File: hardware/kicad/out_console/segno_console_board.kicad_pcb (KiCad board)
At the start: 2 copper layers, 115 x 96 mm, 53 parts, among them J1 RaspberryPi_Pico_SMD_HandSold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, J10 JST_XH_B2B-XH-A_1x02_P2.50mm_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, J11 JST_XH_B2B-XH-A_1x02_P2.50mm_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, J12 JST_XH_B2B-XH-A_1x02_P2.50mm_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, J13 JST_XH_B2B-XH-A_1x02_P2.50mm_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, J14 JST_XH_B2B-XH-A_1x02_P2.50mm_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, J15 JST_XH_B2B-XH-A_1x02_P2.50mm_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, J16 JST_XH_B2B-XH-A_1x02_P2.50mm_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, J17 JST_XH_B2B-XH-A_1x02_P2.50mm_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, J18 JST_XH_B2B-XH-A_1x02_P2.50mm_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, J19 JST_XH_B2B-XH-A_1x02_P2.50mm_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, J2 IDC-Header_2x20_P2.54mm_Verti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, J20 JST_XH_B3B-XH-A_1x03_P2.50mm_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, J21 JST_XH_B3B-XH-A_1x03_P2.50mm_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, J22 PinHeader_2x04_P2.54mm_Vertic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, J3 JST_XH_B4B-XH-A_1x04_P2.50mm_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, J4 JST_XH_B3B-XH-A_1x03_P2.50mm_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, J5 JST_XH_B2B-XH-A_1x02_P2.50mm_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, J6 JST_XH_B8B-XH-A_1x08_P2.50mm_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, J7 JST_XH_B3B-XH-A_1x03_P2.50mm_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, J8 JST_XH_B2B-XH-A_1x02_P2.50mm_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, U1 DIP-14_W7.62mm, U2 DIP-6_W7.62mm

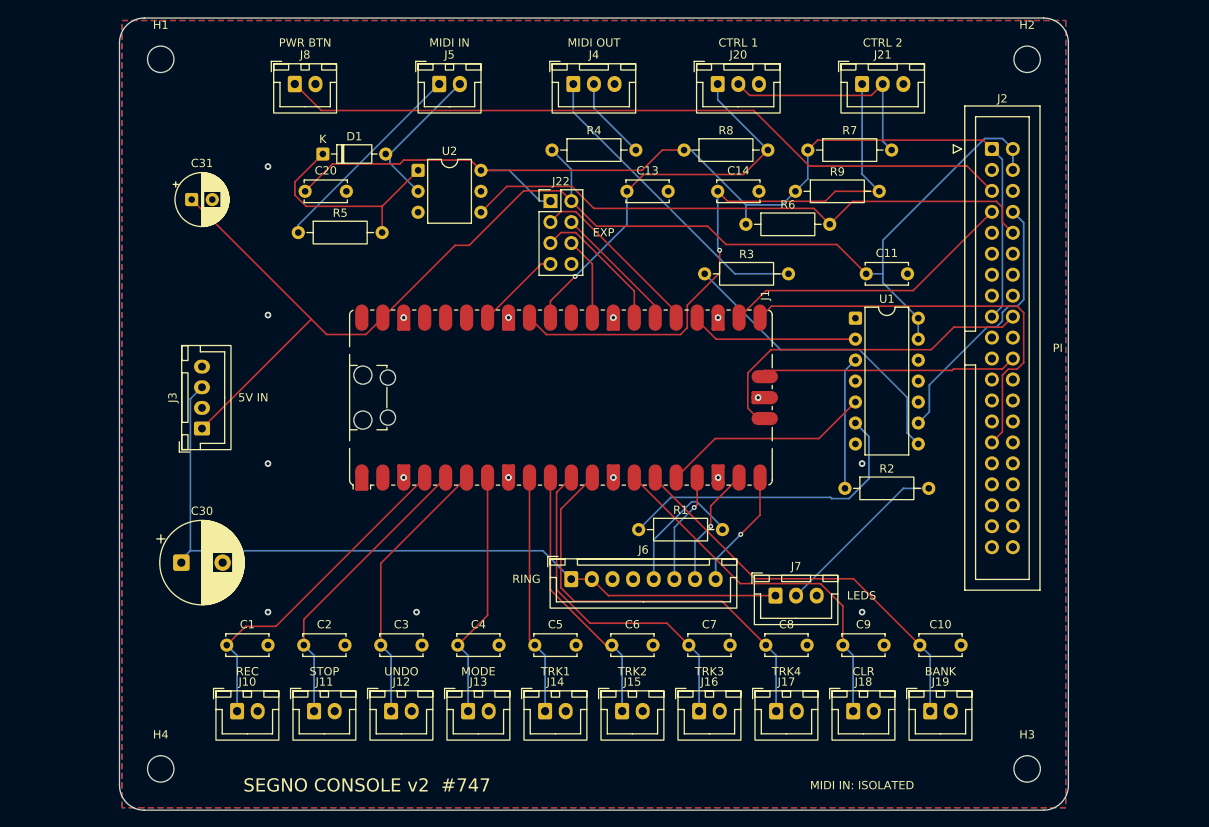
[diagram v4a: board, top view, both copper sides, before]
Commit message: fix(hardware): give the ground pours thermal relief now the Pico is SMD
The pours tied pads with solid copper. That was justified in a comment reading
"THT parts here are hand-soldered, so the usual thermal-relief argument
(wave/reflow) is moot" -- true when written, and false from the commit that made
the Pico a surface-mount module. Its nine GND pads sat in a plane on their own
layer with solid ties, which wicks the iron's heat into the plane and cold-joints
the one part that is painful to rework.

Solid was originally chosen to escape five "starved_thermal" errors from spokes
too narrow to form. That was a symptom of leaving the widths at their defaults,
not a reason to abandon relief: set explicitly (0.3 mm gap, 0.4 mm spokes) there
are none.

Two consequences, both real rather than cosmetic:
- Relief stops pads bridging the pour, which orphaned an F.Cu region. Stitch
  pitch drops 18 -> 12 mm (66 -> 83 vias). Relief and stitch pitch are one
  decision, not two.
- A 3 mm2 minimum island area drops slivers that reach a single pad and go
  nowhere; they cannot carry a return and they fail DRC as starved thermals.

Gated: any pour that ties pads solid while the board carries SMD pads now fails.
Nothing caught this transition, which is why it survived a footprint change.

0 DRC violations, 0 unconnected.

Refs #747
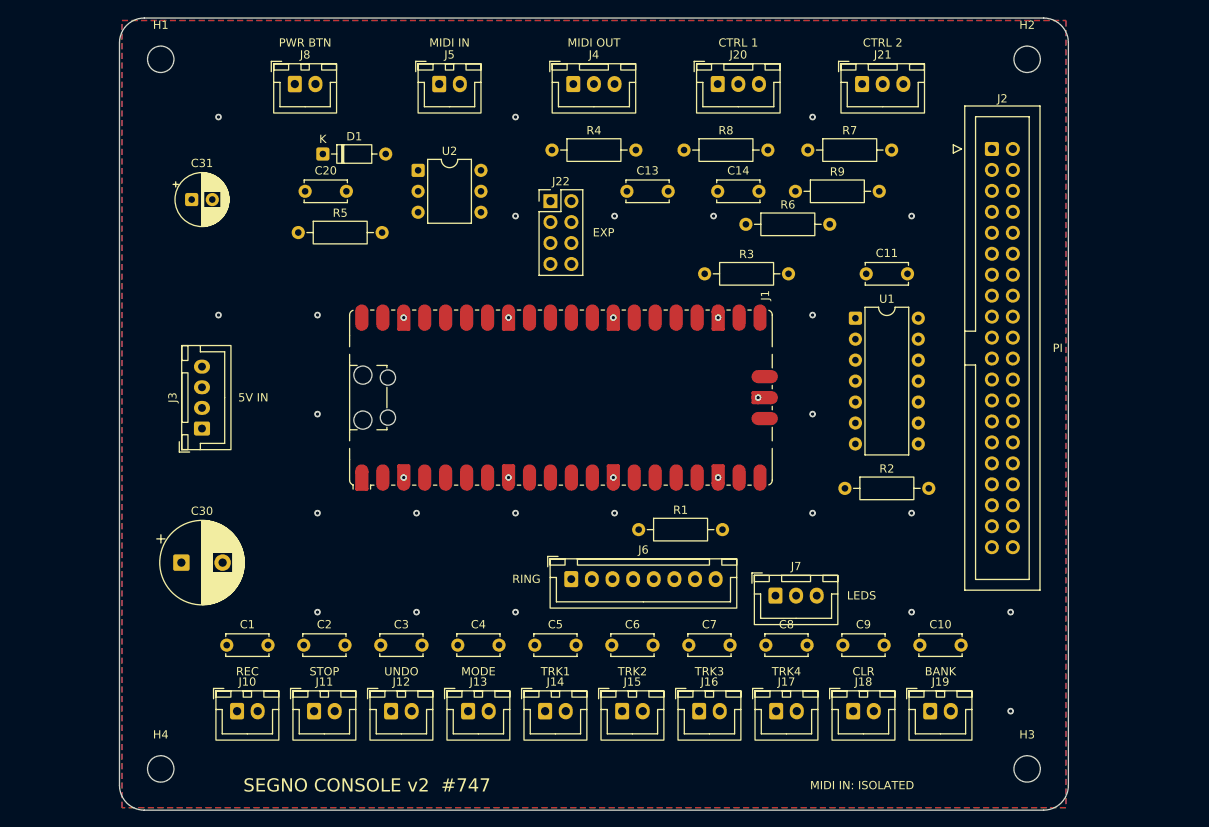
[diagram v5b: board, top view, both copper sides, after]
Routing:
- net +5V: track 165.5 -> 0.00 mm
- net +3V3: track 128.5 -> 0.00 mm
- net +5V_LED: track 95.4 -> 0.00 mm
- net PWR_BTN: track 89.8 -> 0.00 mm
- net CTRL2_TIP: track 73.0 -> 0.00 mm, vias 1 -> 0
- net MIDI_RX: track 71.5 -> 0.00 mm
- net SW_TRACK4: track 51.2 -> 0.00 mm
- net LINK_TX: track 50.8 -> 0.00 mm
- net SW_BANK: track 49.1 -> 0.00 mm
- net CTRL1_TIP: track 48.8 -> 0.00 mm, vias 1 -> 0
- net SW_CLEAR: track 45.0 -> 0.00 mm
- net SW_TRACK3: track 41.7 -> 0.00 mm
- net SWCLK: track 41.0 -> 0.00 mm
- net SW_RECPLAY: track 40.9 -> 0.00 mm
- net RING_DATA_BUF: track 38.0 -> 0.00 mm
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
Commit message: fix(hardware): keep the module's USB corridor clear, and align J6 with J7
The 5 V inlet sat directly in front of the Pico's USB socket. The argument for
pointing that end into the bulk caps was that USB is not NEEDED -- VSYS is fed
from J3 and the Pi flashes over SWD -- but "not needed" quietly became "made
impossible", which is a different claim and not one anyone agreed to. J3 moves
down the left edge and C30 moves up, leaving y 40..52 clear from the socket to
the board edge.

Gated, with a negative control that reproduces exactly the shipped mistake:
anything intruding on the corridor off the module's USB end now fails.

Also J6 (RING) and J7 (LEDS) sat at y 68 and 70 -- same footprint family, side by
side, two millimetres apart for no reason. Both on 69.

0 DRC violations, 0 unconnected.

Refs #747
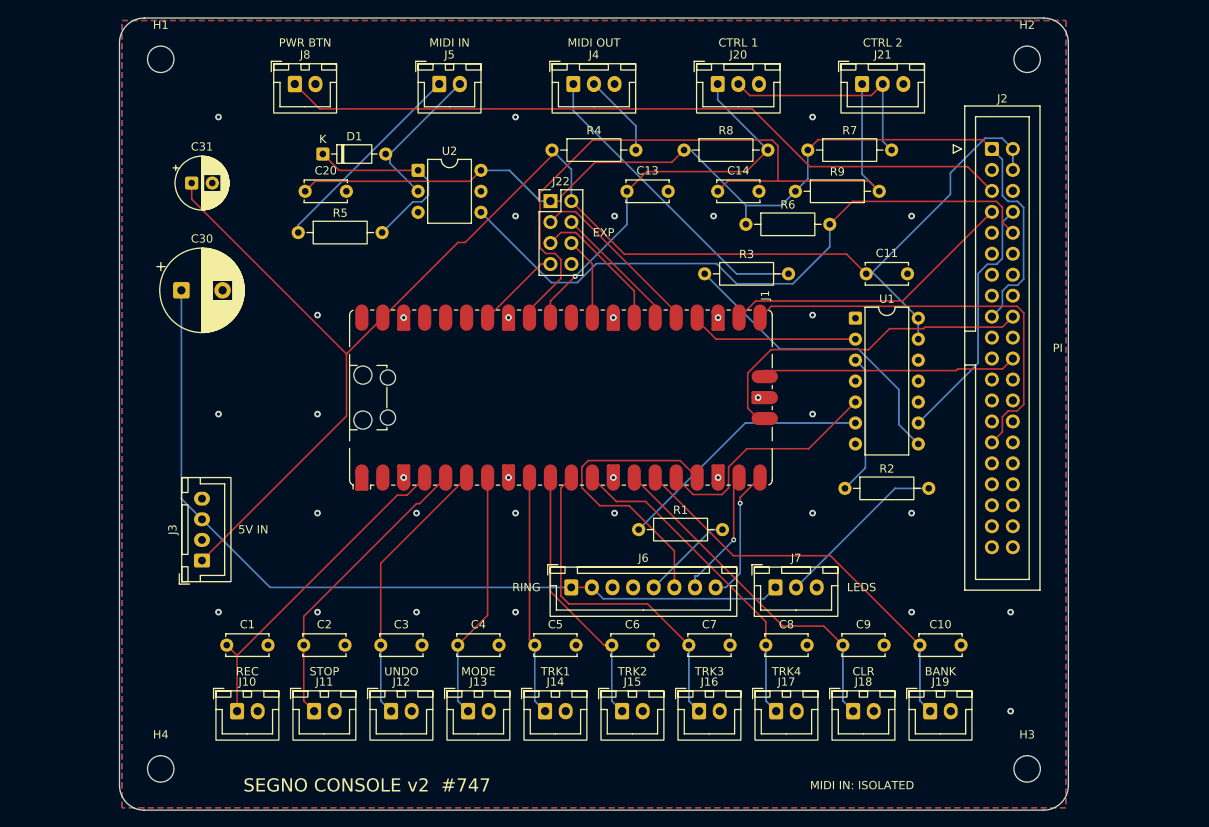
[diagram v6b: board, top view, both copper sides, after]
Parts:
- moved C30 33.0 mm to (107.5, 93.0)
- moved J3 16.0 mm to (110.0, 125.8)
- moved C31 2.00 mm to (108.8, 80.0)
- moved J6 1.00 mm to (154.8, 129.0)
- moved J7 1.00 mm to (179.5, 129.0)
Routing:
- net +5V: track 0.00 -> 182.4 mm
- net +3V3: track 0.00 -> 124.4 mm
- net +5V_LED: track 0.00 -> 102.8 mm
- net PWR_BTN: track 0.00 -> 89.8 mm
- net CTRL2_TIP: track 0.00 -> 88.9 mm
- net MIDI_RX: track 0.00 -> 78.3 mm
- net LINK_TX: track 0.00 -> 50.8 mm
- net SW_BANK: track 0.00 -> 49.0 mm
- net CTRL1_TIP: track 0.00 -> 48.8 mm, vias 0 -> 1
- net SW_CLEAR: track 0.00 -> 42.2 mm
- net SW_TRACK3: track 0.00 -> 41.4 mm
- net SWCLK: track 0.00 -> 41.0 mm
- net SW_RECPLAY: track 0.00 -> 40.2 mm
- net SW_TRACK4: track 0.00 -> 39.6 mm
- net N$1: track 0.00 -> 37.5 mm
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
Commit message: fix(hardware): merge the 5V rails; stop DRC hiding warnings
J3 becomes two parallel +5V/GND pairs instead of a +5V / +5V_LED split. Both
rails came off the same buck, so it was never redundancy or headroom, and the
IR-drop isolation it claimed was half undone by GND being a single pour. Doubling
the contacts buys the thing that is actually scarce: JST XH is ~3 A per contact.
The ring board is unaffected -- it names its own single supply +5V_LED locally,
and two netlists joined by a cable need only agree on pin order, which J6 keeps.

Separately, and worse: the DRC step ran --severity-error, so every '0 violations'
this pipeline has reported was errors-only. The board carries 131 warnings --
100 holes_co_located, 30 via_dangling, 1 starved_thermal. Now --severity-all.

Refs #747
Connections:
- C30 pad 1: +5V_LED -> +5V
- J3 pad 3: +5V_LED -> +5V
- J6 pad 1: +5V_LED -> +5V
- J6 pad 2: +5V_LED -> +5V
- J7 pad 1: +5V_LED -> +5V
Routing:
- net +5V_LED: track 102.8 -> 0.00 mm
- net +5V: track 182.4 -> 261.4 mm
- net RING_DATA: track 28.7 -> 54.8 mm
- net ENC_A: track 36.4 -> 14.5 mm
- net CTRL2_TIP: track 88.9 -> 76.2 mm
- net SW_TRACK4: track 39.6 -> 51.8 mm
- net SW_TRACK3: track 41.4 -> 49.4 mm
- net RING_DATA_BUF: track 31.6 -> 38.5 mm
- net SW_BANK: track 49.0 -> 52.7 mm
- net +3V3: track 124.4 -> 121.0 mm
- net SW_CLEAR: track 42.2 -> 45.4 mm, vias 0 -> 1
- net MIDI_RX: track 78.3 -> 76.9 mm
- net IND_DATA_BUF: track 17.1 -> 16.1 mm
- net ENC_B: track 15.7 -> 15.5 mm, vias 1 -> 0
- net ENC_SW: vias 1 -> 0

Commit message: fix(hardware): the four electrical blockers from the pre-fab review
- ENCODER LEVELS. ring_board.py pulled ENC_A/ENC_B up to its 5 V rail; those land
  on GP13/GP14, whose absolute maximum is 3.6 V. Correct when the far end was
  main_board.py's 5 V Pro Micro, wrong from the day it became a Pico. The pull-ups
  move to this board at 3V3 (and ENC_SW gains the one it never had). New
  PICO_LEVELS gate: PI_LEVELS only ever guarded the Pi, so no check on either
  board could see this.
- PI 5 V. Header pins 2/4 are no longer connected. Tying them put the external
  buck in hard parallel with the Pi 5's PMIC rail with no ORing diode, and after
  the rail merge it put the whole WS2812 load on the Pi's 5 V pin -- which
  segno_console_shopping_list.md forbids in as many words. Gated.
- POWER BUTTON. GPIO3 wakes a Pi 4, not a Pi 5, where the GPIO sits behind RP1
  and the PMIC owns power-on. The button passes through to the Pi's own J2 solder
  pads via J9. The old gate asserted the false version and enforced it all design.
- CTRL REFERENCE. One 1k per jack, not one shared. Shared, a TS footswitch in
  either jack pulled the other jack's pot top to ground.

Also: track width 0.2 -> 0.6 mm (Freerouting reads widths from the DSN netclass,
so TRACK_W/TRACK_PWR were decorative and +5V carried ~1 A on 0.5 A copper);
export() refuses to plot a board with no tracks; --severity-all everywhere.

Refs #747
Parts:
- added J9: JST_XH_B2B-XH-A_1x02_P2.50mm_Vertical, JST_XH_B2B-XH-A_1x02_P2.50mm_Vertical, F.Cu at (126.8, 90.0)
- added R10: R_Axial_DIN0207_L6.3mm_D2.5mm_P10.16mm_Horizontal, R_Axial_DIN0207_L6.3mm_D2.5mm_P10.16mm_Horizontal, F.Cu at (161.7, 85.8)
- added R11: R_Axial_DIN0207_L6.3mm_D2.5mm_P10.16mm_Horizontal, R_Axial_DIN0207_L6.3mm_D2.5mm_P10.16mm_Horizontal, F.Cu at (118.9, 122.0)
- added R12: R_Axial_DIN0207_L6.3mm_D2.5mm_P10.16mm_Horizontal, R_Axial_DIN0207_L6.3mm_D2.5mm_P10.16mm_Horizontal, F.Cu at (132.9, 122.0)
- added R13: R_Axial_DIN0207_L6.3mm_D2.5mm_P10.16mm_Horizontal, R_Axial_DIN0207_L6.3mm_D2.5mm_P10.16mm_Horizontal, F.Cu at (146.9, 122.0)
- moved R5 14.3 mm to (135.7, 89.0)
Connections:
- J2 pad 2: +5V -> (no net)
- J2 pad 4: +5V -> (no net)
- J2 pad 5: PWR_BTN -> (no net)
- J20 pad 2: CTRL_REF -> J20_REF
- J21 pad 2: CTRL_REF -> J21_REF
- R7 pad 2: CTRL_REF -> J20_REF
- R9 pad 2: CTRL2_TIP -> J21_REF
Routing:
- net +3V3: track 121.0 -> 222.4 mm, vias 0 -> 1
- net PWR_BTN: track 89.8 -> 24.3 mm
- net ENC_A: track 14.5 -> 53.2 mm, vias 0 -> 1
- net +5V: track 261.4 -> 222.6 mm
- net SWDIO: track 31.8 -> 67.3 mm, vias 0 -> 1
- net SWCLK: track 41.0 -> 73.0 mm, vias 0 -> 1
- net ENC_B: track 15.5 -> 47.2 mm, vias 0 -> 2
- net RING_DATA: track 54.8 -> 26.0 mm
- net CTRL_REF: track 27.1 -> 0.00 mm
- net J20_REF: track 0.00 -> 21.9 mm
- net MIDI_TX: track 30.9 -> 52.2 mm
- net CTRL2_TIP: track 76.2 -> 55.3 mm, vias 0 -> 2
- net ENC_SW: track 16.3 -> 34.5 mm, vias 0 -> 1
- net MIDI_RX: track 76.9 -> 92.9 mm
- net N$4: track 23.3 -> 39.2 mm
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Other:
- board text added: "PI PWR"
